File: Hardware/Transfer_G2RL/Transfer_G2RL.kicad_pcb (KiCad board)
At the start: 2 copper layers, 88.3 x 71.4 mm, 20 parts, among them J1 SO-239, J2 SO-239, J3 SO-239, J4 SO-239, J5 Screw_Terminal_01x02, K1 G2RL-1-E, K2 G2RL-1-E

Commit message: Manually merged git branch V2 into main
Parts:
- removed TP1, TP2, TP3, TP4: ~, TestPoint:TestPoint_Pad_3.0x3.0mm
- added H1: MountingHole_Pad, TestPoint:TestPoint_Plated_Hole_D2.0mm, F.Cu at (165.3, 108.7)
- added H2: MountingHole_Pad, TestPoint:TestPoint_Plated_Hole_D2.0mm, F.Cu at (114.0, 91.4)
- added H3: MountingHole_Pad, TestPoint:TestPoint_Plated_Hole_D2.0mm, F.Cu at (109.1, 109.2)
- added H4: MountingHole_Pad, TestPoint:TestPoint_Plated_Hole_D2.0mm, F.Cu at (160.3, 91.4)
- renumbered C2 to C1, C8 to C14, C5 to C2, C4 to C3, C3 to C4, C1 to C5, C7 to C8, J5 to J1, J4 to J5, J2 to J6, J1 to J7, J3 to J8, K1 to K3
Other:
- board text added: "Transfer relay V1 License CC BY-SA wa1hco 2025"
- board text removed: "12V"
- board text removed: "Gnd"
- board text removed: "Transfer relay V2 License CC BY-SA wa1hco 2025"

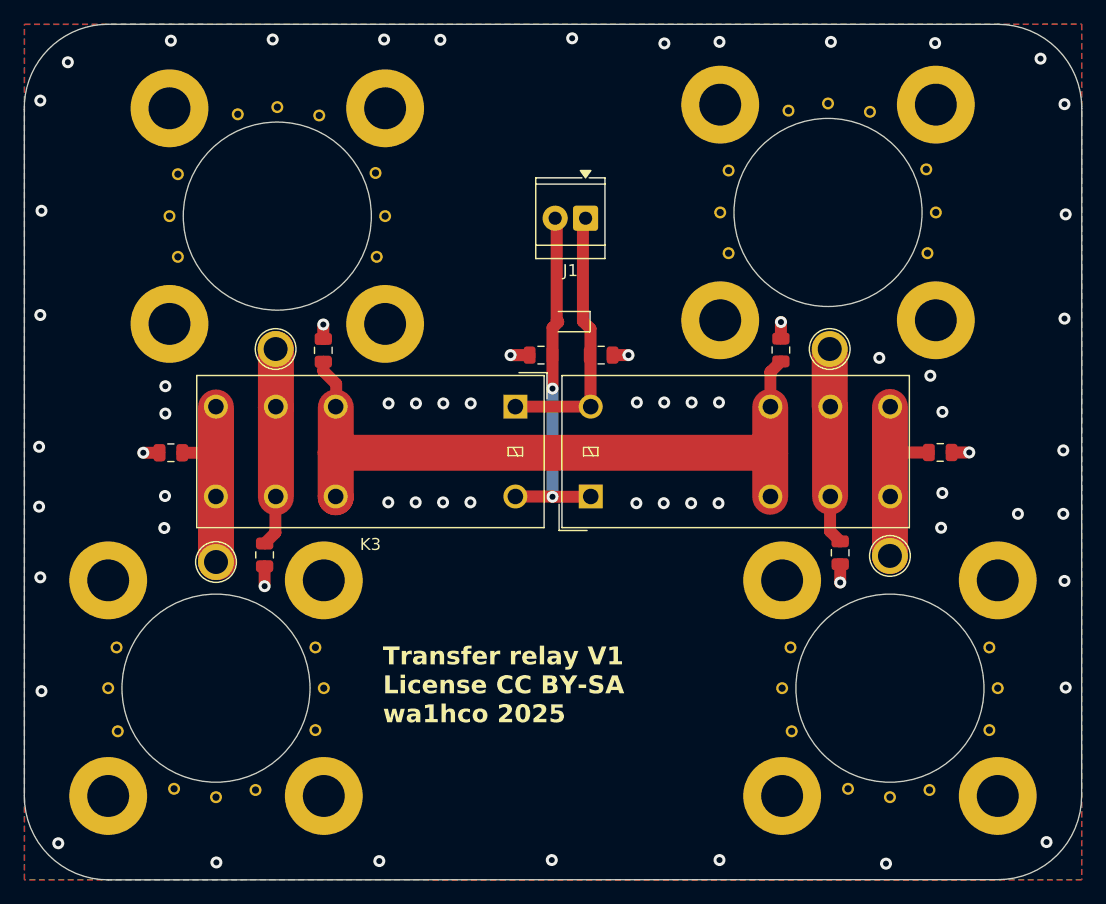
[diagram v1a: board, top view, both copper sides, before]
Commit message: replacing through holes with surface pads for RF to coax center pin wires
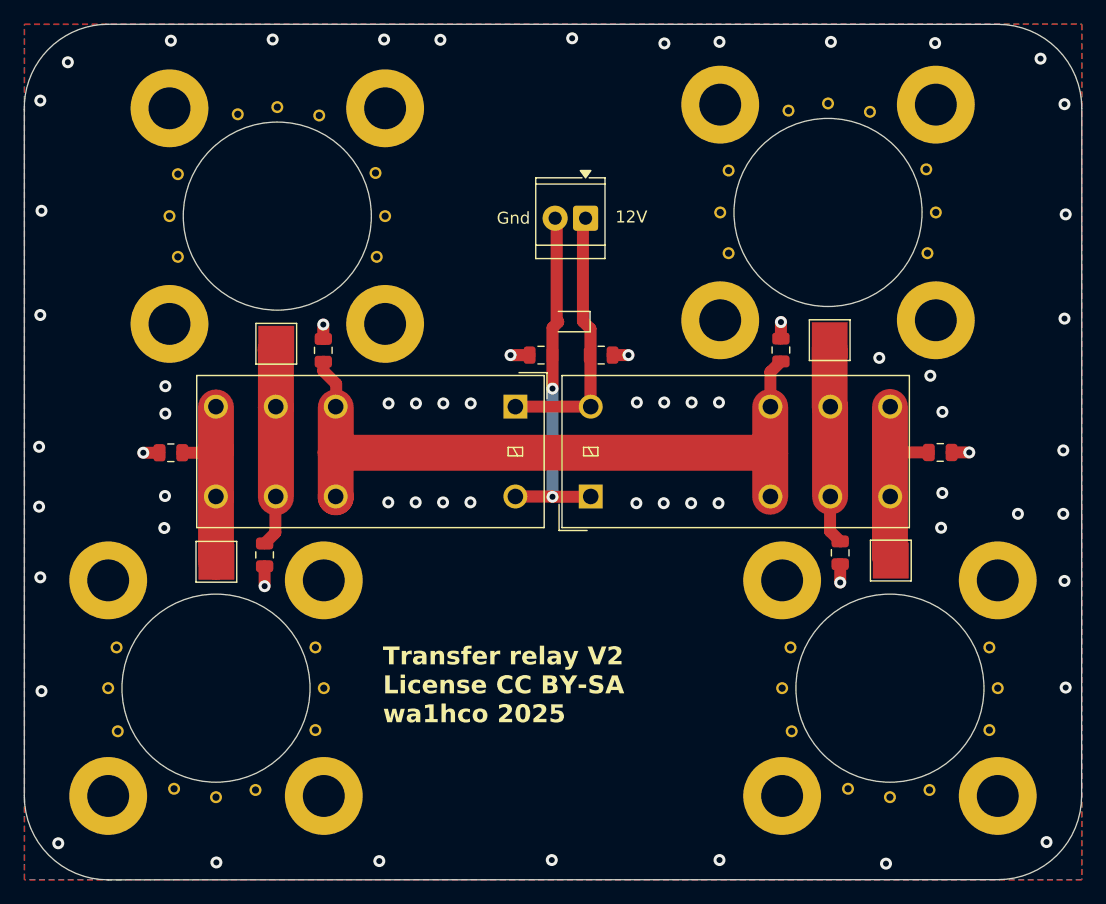
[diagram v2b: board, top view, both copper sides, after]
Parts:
- removed H1, H2, H3, H4: MountingHole_Pad, TestPoint:TestPoint_Plated_Hole_D2.0mm
- added TP1: ~, TestPoint:TestPoint_Pad_3.0x3.0mm, F.Cu at (109.1, 109.2)
- added TP2: ~, TestPoint:TestPoint_Pad_3.0x3.0mm, F.Cu at (165.4, 109.1)
- added TP3: ~, TestPoint:TestPoint_Pad_3.0x3.0mm, F.Cu at (114.1, 91.0)
- added TP4: ~, TestPoint:TestPoint_Pad_3.0x3.0mm, F.Cu at (160.3, 90.7)
- renumbered C5 to C1, C1 to C2, C4 to C3, C3 to C4, C2 to C5, C8 to C7, C14 to C8, J7 to J1, J6 to J2, J8 to J3, J5 to J4, J1 to J5, K3 to K1
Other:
- board text added: "12V"
- board text added: "Gnd"
- board text added: "Transfer relay V2 License CC BY-SA wa1hco 2025"
- board text removed: "Transfer relay V1 License CC BY-SA wa1hco 2025"
